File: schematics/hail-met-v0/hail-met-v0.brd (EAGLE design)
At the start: 77.1 x 61 mm, 110 parts, among them IC1 MCP73871, J1 AVR_SPI_PRG_6PTH, U1 ATMEGA328P, Y1 16MHZ

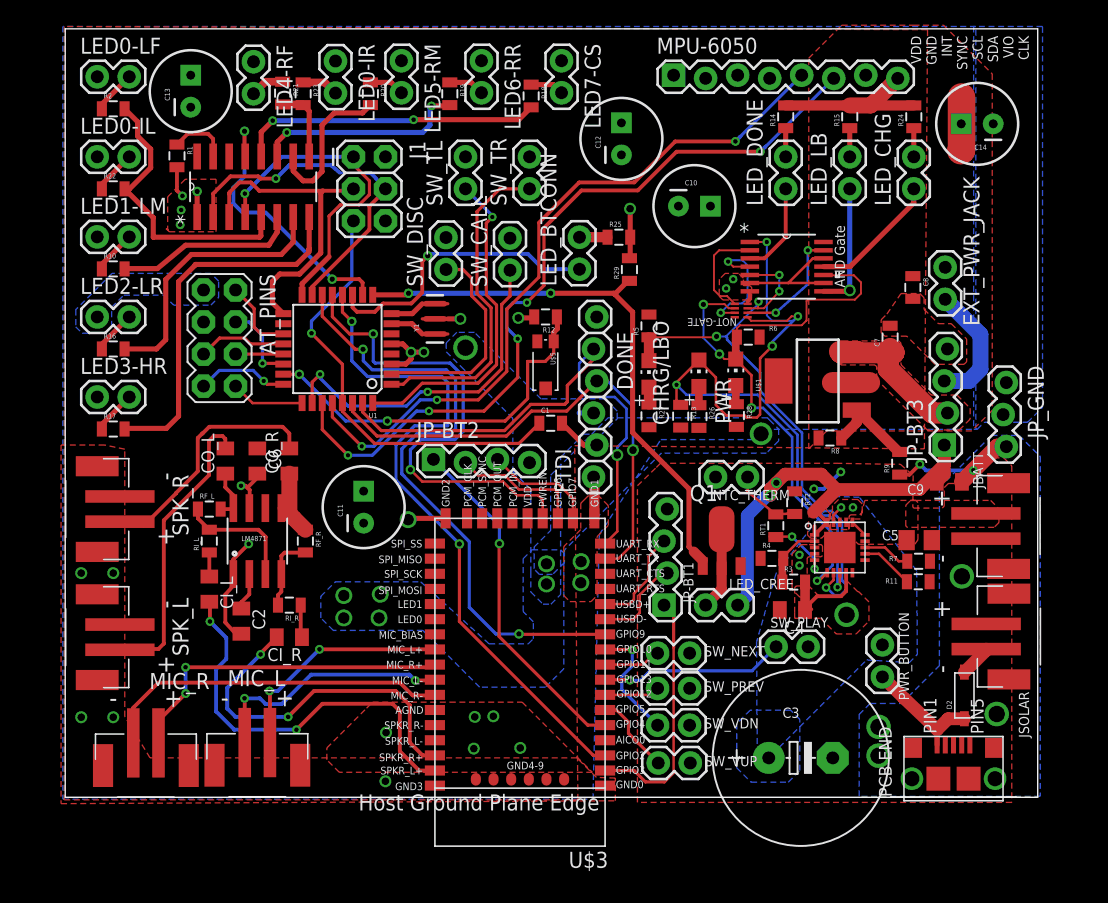
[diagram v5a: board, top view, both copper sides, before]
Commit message: finalized board design, added new npn datasheet
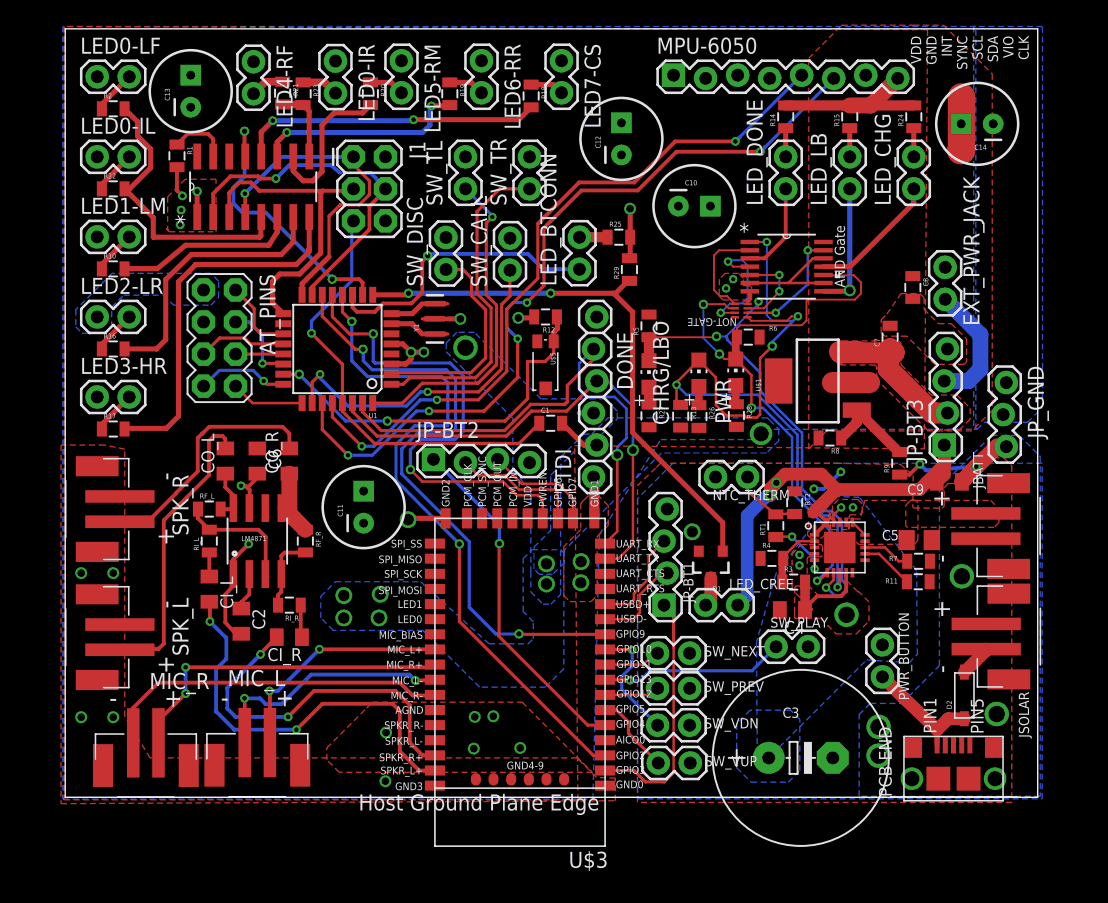
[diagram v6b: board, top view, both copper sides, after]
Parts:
- Q1: device semicon-smd-ipc:SOT89 -> SparkFun:SOT23-3
- moved Q1 2.00 mm to (51.2, 18.5), turned to 180 degrees
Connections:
- net GND: now also Q1.2; no longer Q1.3
- net N$19: now also Q1.3; no longer Q1.2
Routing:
- net N$19: track 3.88 -> 2.34 mm
- net LED_CREE: track 45.3 -> 44.8 mm
- net GND: track 68.5 -> 68.7 mm, vias 34 -> 35
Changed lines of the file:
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@@
 <?xml version="1.0" encoding="utf-8"?>
 <!DOCTYPE eagle SYSTEM "eagle.dtd">
-<eagle version="6.5.0">
+<eagle version="7.1.0">
 <drawing>
 <settings>
@@
 <pass name="Default">
 <param name="RoutingGrid" value="50mil"/>
+<param name="AutoGrid" value="1"/>
+<param name="Efforts" value="0"/>
+<param name="TopRouterVariant" value="1"/>
 <param name="tpViaShape" value="round"/>
 <param name="PrefDir.1" value="|"/>
@@
 <attribute name="VALUE" x="10.16" y="20.32" size="1.27" layer="27" font="vector" rot="R90"/>
 </element>
-<element name="Q1" library="semicon-smd-ipc" package="SOT89" value="" x="52.07" y="20.32"/>
 <element name="JP-BT2" library="SparkFun-Connectors" package="1X04_LOCK" value="" x="29.21" y="26.67"/>
 <element name="JP-BT1" library="SparkFun-Connectors" package="1X04_LOCK" value="" x="47.625" y="15.24" smashed="yes" rot="R90">
@@
 <element name="C13" library="SparkFun-Capacitors" package="CPOL-RADIAL-100UF-25V" value="" x="9.9568" y="56.007" rot="R90"/>
 <element name="C14" library="SparkFun-Capacitors" package="CPOL-RADIAL-100UF-25V" value="" x="72.3392" y="53.4162" rot="R180"/>
+<element name="Q1" library="SparkFun" package="SOT23-3" value="" x="51.2064" y="18.5166" rot="R180"/>
 </elements>
 <signals>
@@
 <contactref element="R1" pad="2"/>
 <contactref element="J1" pad="6"/>
-<contactref element="Q1" pad="3"/>
 <contactref element="LM4871" pad="1"/>
 <contactref element="JP-BT1" pad="4"/>
@@
 </polygon>
 <contactref element="C9" pad="2"/>
-<wire x1="71.1294" y1="25.019" x2="72.0391" y2="25.9287" width="1.27" layer="1"/>
-<wire x1="72.0391" y1="25.9287" x2="73.9234" y2="27.813" width="1.27" layer="1"/>
+<wire x1="71.1294" y1="25.019" x2="72.2677" y2="26.2335" width="1.27" layer="1"/>
+<wire x1="72.2677" y1="26.2335" x2="73.9234" y2="27.813" width="1.27" layer="1"/>
 <wire x1="73.9234" y1="27.813" x2="74.6506" y2="27.813" width="1.27" layer="1"/>
 <polygon width="0.2032" layer="1">
@@
 <via x="67.7926" y="26.416" extent="1-16" drill="0.3556"/>
 <wire x1="67.7926" y1="26.416" x2="68.2799" y2="25.9287" width="0.3048" layer="16"/>
-<wire x1="68.2799" y1="25.9287" x2="72.0391" y2="25.9287" width="0.3048" layer="16"/>
-<via x="72.0391" y="25.9287" extent="1-16" drill="0.3556"/>
+<wire x1="68.2799" y1="25.9287" x2="72.2677" y2="26.2335" width="0.3048" layer="16"/>
+<via x="72.2677" y="26.2335" extent="1-16" drill="0.3556"/>
 <polygon width="0.254" layer="1">
 <vertex x="8.001" y="45.1104"/>
@@
 <wire x1="8.8646" y1="49.9762" x2="8.8646" y2="48.133" width="0.3048" layer="1"/>
 <wire x1="8.8646" y1="48.133" x2="9.2964" y2="47.7012" width="0.3048" layer="1"/>
-<wire x1="74.6506" y1="27.813" x2="74.3966" y2="30.353" width="0" layer="19" extent="1-1"/>
+<contactref element="Q1" pad="2"/>
+<polygon width="0.4064" layer="16" rank="4">
+<vertex x="62.1792" y="26.4922"/>
+<vertex x="48.2092" y="26.4922"/>
+<vertex x="45.4152" y="23.6982"/>
+<vertex x="45.4152" y="-0.127"/>
+<vertex x="48.4886" y="-0.127"/>
+<vertex x="77.4954" y="-0.127"/>
+<vertex x="77.4954" y="24.2316"/>
+<vertex x="77.4954" y="26.4922"/>
+</polygon>
+<via x="49.7332" y="21.0566" extent="1-16" drill="0.9" shape="octagon"/>
+<wire x1="74.3966" y1="30.353" x2="74.6506" y2="27.813" width="0" layer="19" extent="1-1"/>
 </signal>
 <signal name="VIN">
@@
 <wire x1="32.766" y1="31.5214" x2="35.0266" y2="33.782" width="0.254" layer="1"/>
 <wire x1="35.0266" y1="33.782" x2="35.0266" y2="38.7096" width="0.254" layer="1"/>
-<wire x1="35.0266" y1="38.7096" x2="37.5666" y2="41.2496" width="0.254" layer="1"/>
-<wire x1="37.5666" y1="41.2496" x2="37.5666" y2="45.5676" width="0.254" layer="1"/>
+<wire x1="35.0266" y1="38.7096" x2="37.4904" y2="41.148" width="0.254" layer="1"/>
+<wire x1="37.4904" y1="41.148" x2="37.4904" y2="45.4914" width="0.254" layer="1"/>
 <wire x1="53.5432" y1="52.4002" x2="58.42" y2="57.277" width="0.254" layer="16"/>
-<wire x1="37.5666" y1="45.5676" x2="40.767" y2="48.768" width="0.3048" layer="1"/>
+<wire x1="37.4904" y1="45.4914" x2="40.767" y2="48.768" width="0.3048" layer="1"/>
 <wire x1="40.767" y1="48.768" x2="45.1358" y2="48.768" width="0.3048" layer="1"/>
 <wire x1="45.1358" y1="48.768" x2="48.387" y2="52.0192" width="0.3048" layer="1"/>
@@
 </signal>
 <signal name="N$19">
-<contactref element="Q1" pad="2"/>
 <contactref element="LED_CREE" pad="2"/>
-<wire x1="52.07" y1="18.593" x2="52.07" y2="16.51" width="0.8128" layer="1"/>
-<wire x1="52.07" y1="16.51" x2="50.8" y2="15.24" width="0.8128" layer="1"/>
+<contactref element="Q1" pad="3"/>
+<wire x1="51.2064" y1="17.4166" x2="51.2064" y2="15.6464" width="1.016" layer="1"/>
+<wire x1="51.2064" y1="15.6464" x2="50.8" y2="15.24" width="1.016" layer="1"/>
 </signal>
 <signal name="LED_CREE">
 <contactref element="U1" pad="9"/>
-<wire x1="50.571" y1="18.771" x2="49.8602" y2="19.4818" width="0.8128" layer="1"/>
-<wire x1="49.8602" y1="19.4818" x2="49.4792" y2="19.8628" width="0.4064" layer="1"/>
-<wire x1="49.4792" y1="19.8628" x2="49.4792" y2="24.4602" width="0.4064" layer="1"/>
-<wire x1="49.4792" y1="24.4602" x2="45.0088" y2="28.9306" width="0.4064" layer="1"/>
+<wire x1="52.1564" y1="21.783" x2="45.0088" y2="28.9306" width="0.4064" layer="1"/>
 <wire x1="45.0088" y1="28.9306" x2="45.0088" y2="38.481" width="0.4064" layer="1"/>
 <wire x1="45.0088" y1="38.481" x2="43.5864" y2="39.9034" width="0.4064" layer="1"/>
@@
 <wire x1="27.2288" y1="39.9796" x2="27.1018" y2="39.8526" width="0.4064" layer="1"/>
 <wire x1="27.1018" y1="39.8526" x2="24.39" y2="39.8526" width="0.4064" layer="1"/>
-<contactref element="Q1" pad="1"/>
 <contactref element="R29" pad="1"/>
 <wire x1="44.7548" y1="40.9592" x2="44.6422" y2="40.9592" width="0.4064" layer="1"/>
 <wire x1="44.6422" y1="40.9592" x2="43.5864" y2="39.9034" width="0.4064" layer="1"/>
-<wire x1="50.571" y1="18.771" x2="50.571" y2="18.339" width="0.3048" layer="1"/>
+<contactref element="Q1" pad="1"/>
+<wire x1="52.1564" y1="21.783" x2="52.1564" y2="19.5166" width="0.4064" layer="1"/>
 </signal>
 <signal name="PC1">

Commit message: ordered pcb
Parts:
- renumbered LED0-IR to LED4-IR
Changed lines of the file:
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@@
 <?xml version="1.0" encoding="utf-8"?>
 <!DOCTYPE eagle SYSTEM "eagle.dtd">
-<eagle version="7.1.0">
+<eagle version="6.5.0">
 <drawing>
 <settings>
@@
 <wire x1="77.14" y1="60.95" x2="0" y2="60.95" width="0" layer="20"/>
 <wire x1="0" y1="60.95" x2="0" y2="0" width="0" layer="20"/>
-<dimension x1="0" y1="60.95" x2="77.14" y2="60.95" x3="38.57" y3="68.58" textsize="1.778" layer="21" unit="inch"/>
-<dimension x1="77.14" y1="60.95" x2="77.47" y2="0" x3="100.157453125" y3="30.59873125" textsize="1.778" layer="21" unit="inch"/>
+<dimension x1="0" y1="60.95" x2="77.14" y2="60.95" x3="38.57" y3="68.58" textsize="1.778" layer="19" unit="inch"/>
+<dimension x1="77.14" y1="60.95" x2="77.47" y2="0" x3="100.157453125" y3="30.59873125" textsize="1.778" layer="19" unit="inch"/>
 <text x="67.0814" y="60.4012" size="0.8128" layer="25" rot="R90" align="top-right">VDD
 GND
@@
 <pass name="Default">
 <param name="RoutingGrid" value="50mil"/>
-<param name="AutoGrid" value="1"/>
-<param name="Efforts" value="0"/>
-<param name="TopRouterVariant" value="1"/>
 <param name="tpViaShape" value="round"/>
 <param name="PrefDir.1" value="|"/>
@@
 <element name="C8" library="SparkFun-Passives" package="0805" value="22pF" x="67.2338" y="40.4368" rot="R270"/>
 <element name="CHRG/LBO" library="adafruit" package="CHIP-LED0805" value="ORANGE" x="50.2666" y="33.6296" smashed="yes">
-<attribute name="NAME" x="47.879" y="29.5148" size="1.27" layer="25" rot="R90"/>
+<attribute name="NAME" x="49.5046" y="31.9532" size="0.8128" layer="25" rot="R90"/>
 </element>
 <element name="DONE" library="adafruit" package="CHIP-LED0805" value="GREEN" x="46.3042" y="33.5788" smashed="yes">
-<attribute name="NAME" x="45.0342" y="32.3088" size="1.27" layer="25" rot="R90"/>
+<attribute name="NAME" x="45.0342" y="32.3088" size="0.8128" layer="25" rot="R90"/>
 </element>
 <element name="FTDI" library="SparkFun-Connectors" package="1X06_LOCK" value="" x="41.91" y="25.4" rot="R90"/>
 <element name="IC1" library="adafruit" package="QFN20" value="MCP73871" x="61.4426" y="19.812" smashed="yes"/>
 <element name="LED_CREE" library="SparkFun-Connectors" package="1X02" value="M02PTH" x="53.34" y="15.24" smashed="yes" rot="R180">
-<attribute name="NAME" x="52.6542" y="16.51" size="0.8128" layer="25" ratio="10"/>
+<attribute name="NAME" x="49.0982" y="13.0048" size="0.8128" layer="25" ratio="10"/>
 </element>
 <element name="LED0-IL" library="SparkFun-Connectors" package="1X02" value="M02PTH" x="2.54" y="50.8" smashed="yes">
 <attribute name="NAME" x="1.1938" y="52.6288" size="1.27" layer="25" ratio="10"/>
 </element>
-<element name="LED0-IR" library="SparkFun-Connectors" package="1X02" value="M02PTH" x="21.4376" y="58.3946" smashed="yes" rot="R270">
+<element name="LED4-IR" library="SparkFun-Connectors" package="1X02" value="M02PTH" x="21.4376" y="58.3946" smashed="yes" rot="R270">
 <attribute name="NAME" x="23.2664" y="59.7408" size="1.27" layer="25" ratio="10" rot="R270"/>
 </element>
@@
 </element>
 <element name="PWR" library="adafruit" package="CHIP-LED0805" value="RED" x="53.1876" y="33.7058" smashed="yes">
-<attribute name="NAME" x="52.832" y="29.6164" size="1.27" layer="25" rot="R90"/>
+<attribute name="NAME" x="52.2986" y="32.3342" size="0.8128" layer="25" rot="R90"/>
 </element>
 <element name="R1" library="SparkFun-Passives" package="0805" value="" x="8.8646" y="50.8762" smashed="yes" rot="R270">
@@
 <attribute name="PROD_ID" value="XTAL-08900" x="29.337" y="37.9476" size="1.778" layer="27" rot="R90" display="off"/>
 </element>
-<element name="U$3" library="RN52" package="RN52" value="RN52" x="42.8244" y="22.1234" rot="R180">
+<element name="U$3" library="RN52" package="RN52" value="RN52" x="42.8244" y="22.1234" smashed="yes" rot="R180">
 <attribute name="DIGIKEY_OC" value="RN52-I/RM-ND" x="42.8244" y="22.1234" size="1.778" layer="27" rot="R180" display="off"/>
+<attribute name="NAME" x="43.0744" y="-4.3266" size="1.27" layer="21" rot="R180"/>
 </element>
 <element name="U$2" library="MicroUSB" package="10118193" value="10118193" x="70.4596" y="1.4732" smashed="yes">
@@
 </element>
 <element name="SW_PLAY" library="SparkFun-Connectors" package="1X02" value="M02PTH" x="56.388" y="11.938" smashed="yes">
-<attribute name="NAME" x="55.9308" y="13.462" size="0.8128" layer="25" ratio="10"/>
+<attribute name="NAME" x="61.2902" y="9.1186" size="0.8128" layer="25" ratio="10" rot="R90"/>
 </element>
 <element name="EXT_PWR_JACK" library="SparkFun-Connectors" package="1X02" value="M02PTH" x="69.7992" y="39.497" smashed="yes" rot="R90">
@@
 <attribute name="SUPPLIER" value="Texas Instruments" x="53.6194" y="38.608" size="1.778" layer="27" rot="R180" display="off"/>
 <attribute name="OC_FARNELL" value="-" x="53.6194" y="38.608" size="1.778" layer="27" rot="R180" display="off"/>
-<attribute name="NAME" x="53.2638" y="37.9984" size="0.6096" layer="25" ratio="10" rot="SR180"/>
+<attribute name="NAME" x="55.7276" y="37.8206" size="0.6096" layer="25" ratio="10" rot="SR180"/>
 </element>
 <element name="D2" library="adafruit" package="SOD-123" value="" x="71.3232" y="8.0772" rot="R90"/>
@@
 <contactref element="LED4-RF" pad="1"/>
 <contactref element="LED0-IL" pad="1"/>
-<contactref element="LED0-IR" pad="1"/>
+<contactref element="LED4-IR" pad="1"/>
 <contactref element="LM4871" pad="6"/>
 <contactref element="C6" pad="1"/>
@@
 </signal>
 <signal name="N$66">
-<contactref element="LED0-IR" pad="2"/>
+<contactref element="LED4-IR" pad="2"/>
 <contactref element="R23" pad="1"/>
 <wire x1="18.8722" y1="56.7038" x2="20.5884" y2="56.7038" width="0.6096" layer="1"/>
